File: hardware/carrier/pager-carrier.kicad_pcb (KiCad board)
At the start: 2 copper layers, 46.2 x 51 mm, 89 parts, among them J1 PANEL, J2 CARDKB, J3 HAPTIC, J4 EXT_LED, J5 PIEZ, J6 USB4235, J7 BATTERY, M1 Walter, Q1 UMH3N, Q2 SI1308EDL, Q3 MMST3904, Q4 AO3401A, SW1 KMR221GLFS, SW2 JS102011SAQN, U1 CP2102N-A02-GQFN24, U2 SN74LVC2G126DCUR, U3 DRV2605LDGSR, U4 LIS2DW12TR, U5 BQ25185DLHR, U6 MAX17048G+T10, U7 TPS62840DLCR

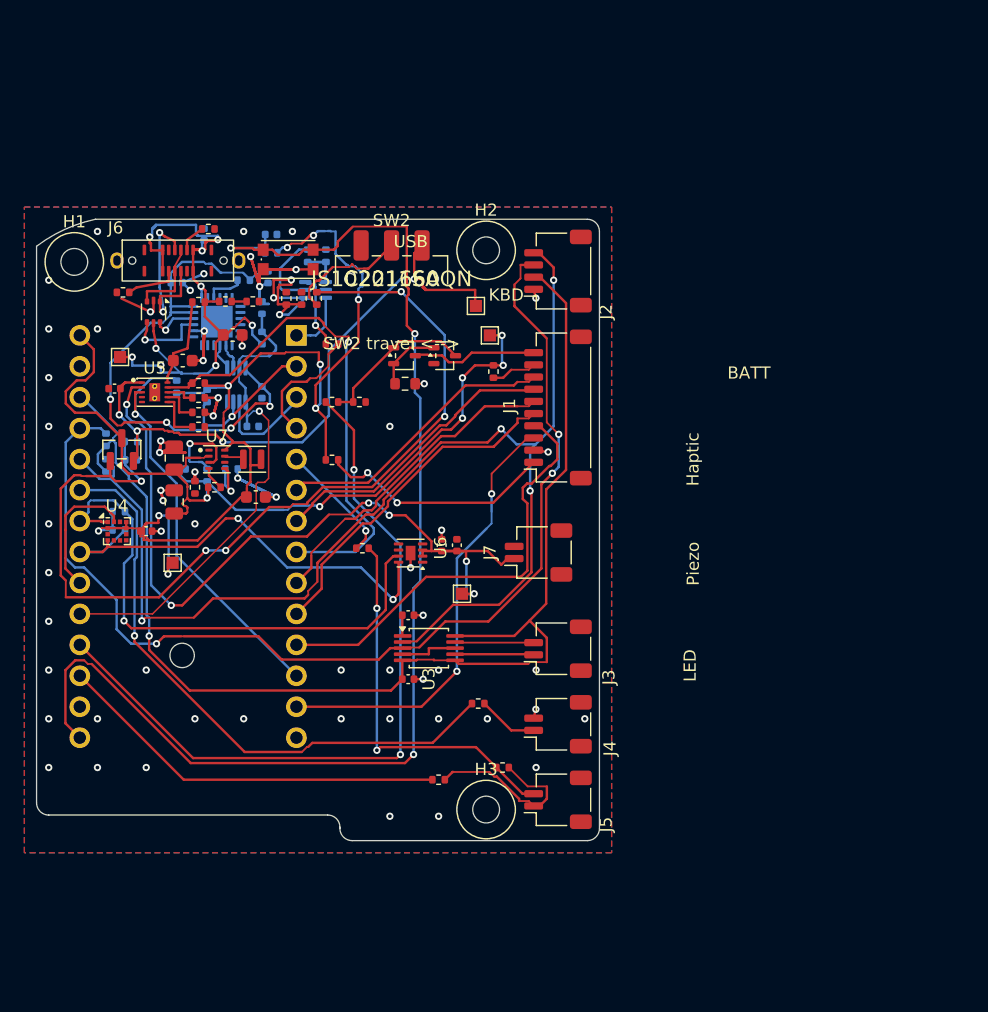
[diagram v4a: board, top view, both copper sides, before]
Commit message: Carrier: hand-layout in progress, USB circuit first (owner)
Autorouted tracks ripped up (1059 -> 448 segments, 149 -> 41 vias) for the
all-top-side hand layout. R35/R36 (U7 MODE 0R straps) removed from the schematic
and board. STEP re-exported.

Co-Authored-By: Claude Fable 5.1 <noreply@anthropic.com>
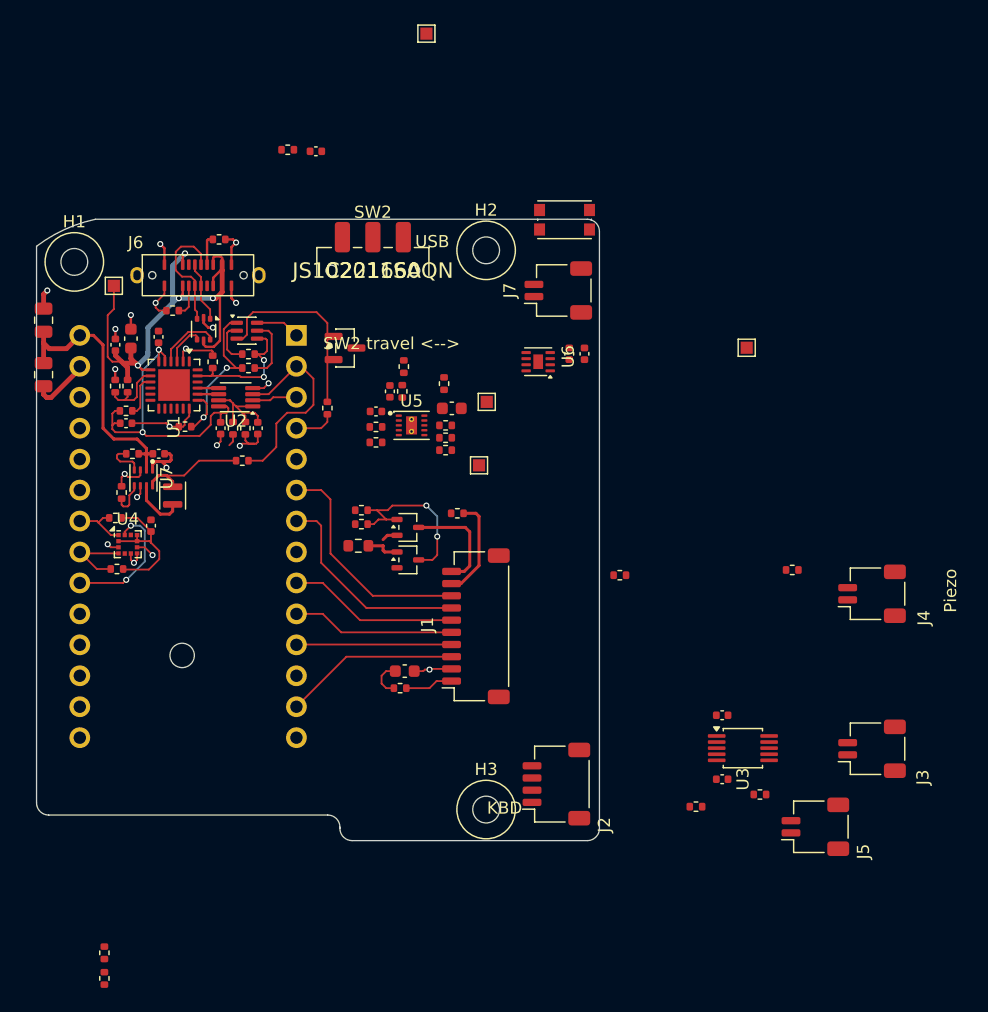
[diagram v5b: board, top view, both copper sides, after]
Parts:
- removed R35, R36: 0R, Resistor_SMD:R_0402_1005Metric
- C14, C18, C19, C2, C3, C4, C5, C9, Q1, R14, R15, R16, R17, R18, R28, R3, R32, R33, R34, R38, R5, R6, R7, U1, U2: moved to F.Cu
- moved TP10 46.1 mm to (106.3, 42.2)
- moved R16 42.1 mm to (79.9, 119.7), turned to -90 degrees
- moved J2 42.1 mm to (117.0, 103.8)
- moved R15 42.1 mm to (79.9, 117.6), turned to -90 degrees
- moved R21 28.0 mm to (136.3, 86.2)
- moved J4 27.9 mm to (142.9, 88.1)
- moved J3 27.1 mm to (142.9, 100.9)
- moved U3 27.1 mm to (132.3, 100.8)
- moved C10 27.1 mm to (130.6, 103.4)
- moved C11 27.1 mm to (130.6, 98.1)
- moved TP11 26.4 mm to (110.6, 77.6)
- moved SW1 22.9 mm to (117.6, 57.4)
- moved R32 22.6 mm to (104.3, 71.5), turned to -90 degrees
- moved C13 22.4 mm to (108.4, 72.9)
- moved C14 22.0 mm to (103.3, 71.5), turned to -90 degrees
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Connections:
- U7 pad 3: Net-(U7-MODE) -> GND
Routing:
- net 3V3_AWK: track 104.6 -> 0.00 mm, vias 1 -> 0
- net /Core/FL_BTN: track 103.2 -> 0.00 mm, vias 3 -> 0
- net /Core/AWK_SCL: track 99.5 -> 0.00 mm, vias 4 -> 0
- net /Core/AWK_SDA: track 89.3 -> 0.00 mm, vias 3 -> 0
- net Net-(Q4-G): track 77.4 -> 0.00 mm, vias 5 -> 0
- net 3V3: track 89.2 -> 24.0 mm, vias 9 -> 0
- net GND: track 115.9 -> 51.3 mm, vias 62 -> 21
- net VBAT: track 63.4 -> 0.00 mm, vias 6 -> 0
- net /Core/FL_PWM: track 61.8 -> 0.00 mm, vias 2 -> 0
- net SYS: track 54.1 -> 0.00 mm, vias 4 -> 0
- net SYS_SW: track 72.5 -> 22.3 mm, vias 6 -> 0
- net /Core/EXT_LED: track 49.3 -> 0.00 mm, vias 1 -> 0
- net CHG_STAT1: track 42.3 -> 0.00 mm, vias 1 -> 0
- net AON_SCL: track 44.6 -> 4.70 mm, vias 1 -> 0
- net CHG_STAT2: track 35.1 -> 0.00 mm, vias 1 -> 0
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- removed copper zone on B.Cu, net GND
- removed copper zone on F.Cu, net GND
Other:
- board text removed: "BATT"
- board text removed: "Haptic"
- board text removed: "LED"

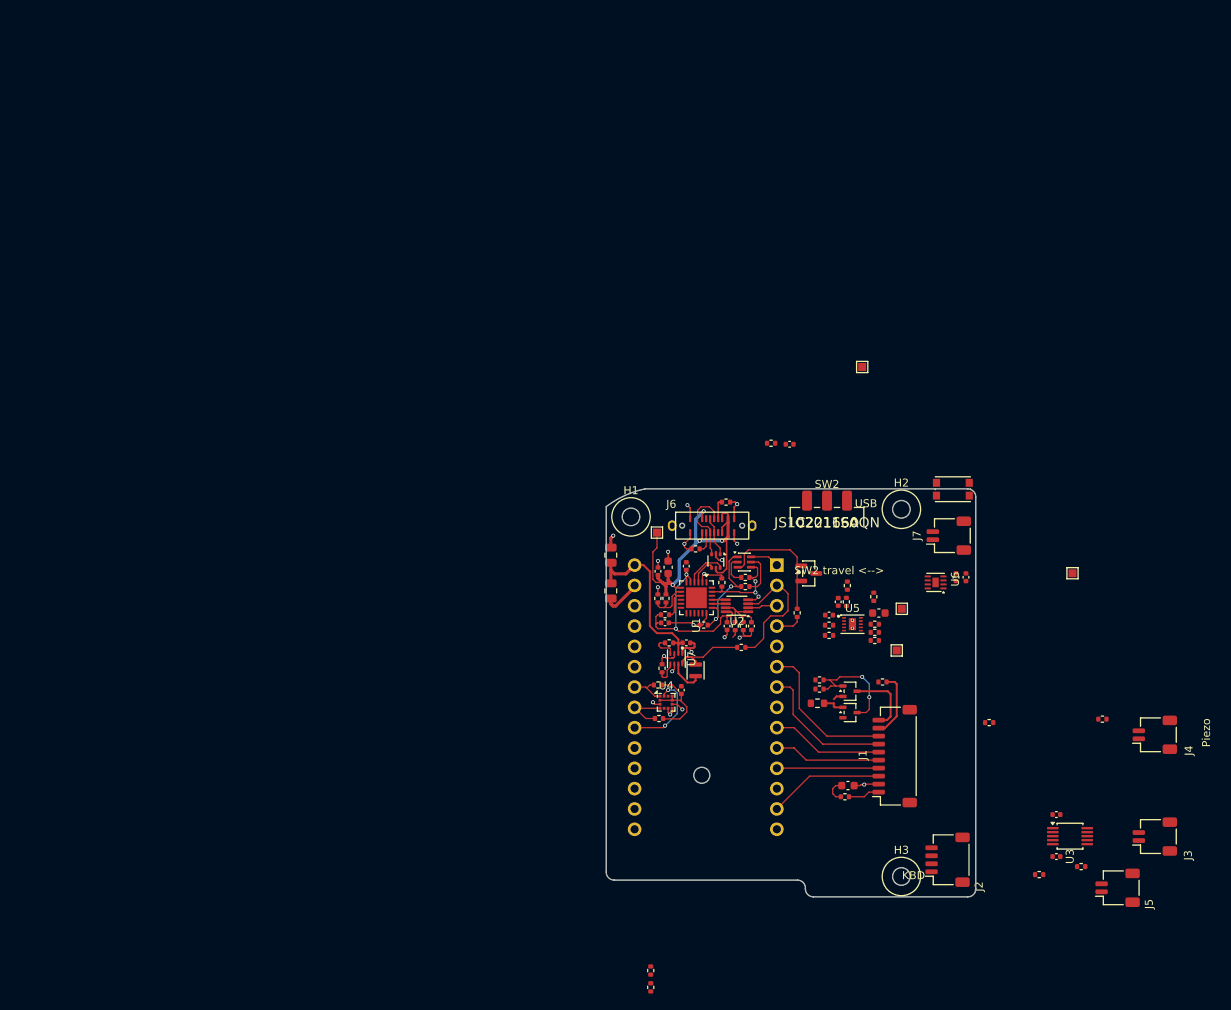
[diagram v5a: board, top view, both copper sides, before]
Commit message: Carrier: hand-layout WIP, Walter pins remapped, panel header J1 10 -> 8 pins (owner)
Co-Authored-By: Claude Fable 5.1 <noreply@anthropic.com>
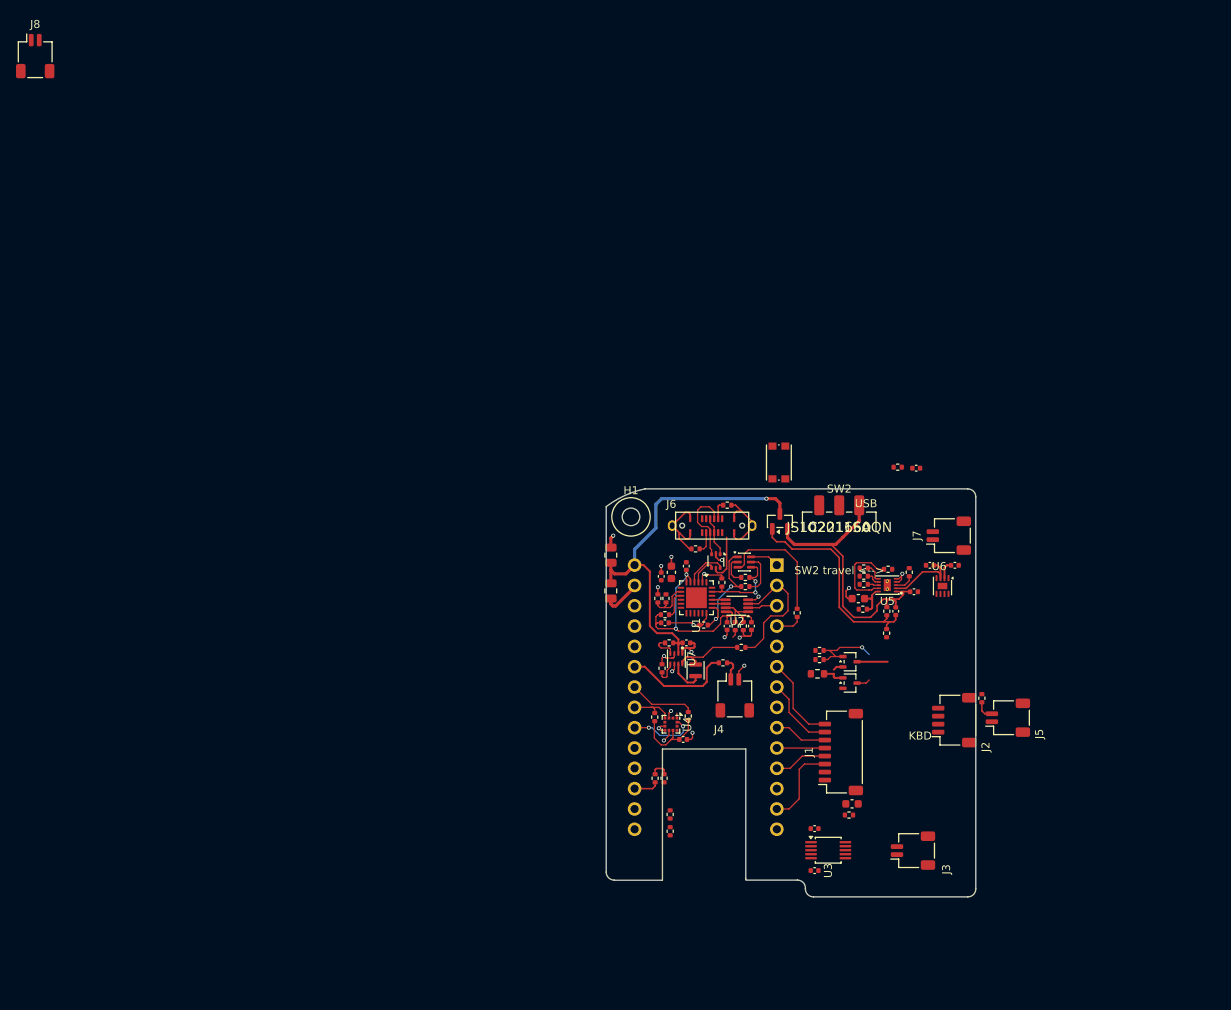
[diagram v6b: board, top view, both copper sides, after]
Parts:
- removed H2, H3: Cassette M2, pager-carrier:MountingHole_2.2mm_M2_Cassette
- removed R13: 0R, Resistor_SMD:R_0402_1005Metric
- removed TP10: VBAT, TestPoint:TestPoint_Pad_1.0x1.0mm
- removed TP11: 3V3, TestPoint:TestPoint_Pad_1.0x1.0mm
- removed TP7: VBUS, TestPoint:TestPoint_Pad_1.0x1.0mm
- removed TP8: SYS, TestPoint:TestPoint_Pad_1.0x1.0mm
- removed TP9: SYS_SW, TestPoint:TestPoint_Pad_1.0x1.0mm
- added J8: FRONTLIGHT, Connector_JST:JST_SH_SM02B-SRSS-TB_1x02-1MP_P1.00mm_Horizontal, F.Cu at (2.92, 3.31)
- J1: footprint Connector_JST:JST_SH_SM10B-SRSS-TB_1x10-1MP_P1.00mm_Horizontal -> Connector_JST:JST_SH_SM08B-SRSS-TB_1x08-1MP_P1.00mm_Horizontal
- moved R22 53.3 mm to (81.5, 93.6), turned to 90 degrees
- moved J4 52.7 mm to (90.4, 83.2), turned to 0 degrees
- moved R19 49.5 mm to (80.4, 93.6), turned to 90 degrees
- moved R21 47.9 mm to (88.9, 79.1)
- moved J3 30.3 mm to (112.6, 102.6)
- moved U3 30.3 mm to (102.0, 102.6)
- moved C10 30.3 mm to (100.3, 105.1)
- moved C11 30.3 mm to (100.3, 99.9)
- moved J5 25.3 mm to (124.5, 86.0)
- moved SW1 22.0 mm to (95.9, 54.1), turned to 90 degrees
- moved R16 19.7 mm to (82.3, 100.2)
- moved R15 19.7 mm to (82.3, 98.1)
- moved J2 17.5 mm to (117.8, 86.3)
- moved C5 16.1 mm to (113.1, 54.8)
- moved R5 16.1 mm to (110.7, 54.7)
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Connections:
- net SYS renamed /Power/SYS
- net VBAT renamed /Power/VBAT
- M1 pad 18: /Core/FL_PWM -> /Core/PIEZ_N
- M1 pad 5: /Core/PIEZ_N -> /Core/FL_PWM
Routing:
- net VBUS: track 44.6 -> 6.90 mm, vias 4 -> 0
- net /Power/SYS: track 0.00 -> 35.6 mm
- net Net-(Q4-G): track 0.00 -> 27.2 mm
- net SYS_SW: track 22.3 -> 48.6 mm, vias 0 -> 1
- net GND: track 51.3 -> 66.0 mm, vias 21 -> 20
- net /Core/EXT_LED: track 0.00 -> 13.8 mm
- net /Power/VBAT: track 0.00 -> 10.8 mm
- net CHG_STAT1: track 0.00 -> 10.3 mm
- net /Core/FL_P: track 8.28 -> 0.00 mm
- net /Core/EINK_RST: track 17.5 -> 9.30 mm
- net /Core/EINK_BUSY: track 18.9 -> 10.8 mm
- net /Core/EINK_CS: track 13.4 -> 6.00 mm
- net /Core/EINK_DC: track 14.0 -> 6.64 mm
- net /Core/EINK_MOSI: track 12.7 -> 6.64 mm
- net /Core/FL_N: track 8.82 -> 3.83 mm
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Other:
- outline, holes or cut-outs redrawn
- board text removed: "Piezo"
